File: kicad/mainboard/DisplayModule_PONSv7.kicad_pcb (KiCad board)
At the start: 4 copper layers, 55.4 x 77.6 mm, 135 parts, among them J1 Ext. Speaker, J2 54132-4062, J3 2005280040, J4 Micro_SD_Card_Det2, J5 Conn_01x03_Shielded, J6 USB_B_Micro, Q1 AO3401A, SW1 PTS645VK392LFS, SW2 SW_TS-1088, SW3 SW_TS-1088, U1 PAM8302AADCR, U10 BNO085, U12 E220-900T22S(JP), U2 W25Q128JVS, U3 RP2350_80QFN, U4 MCP73831-2-OT, U5 TPS63031DSK, U6 MAINSW_CUS-12TB, U7 TFTSW_CUS-12TB, U8 MS5611-01BA, Y1 X322512MSB4SI, Y2 32.768k

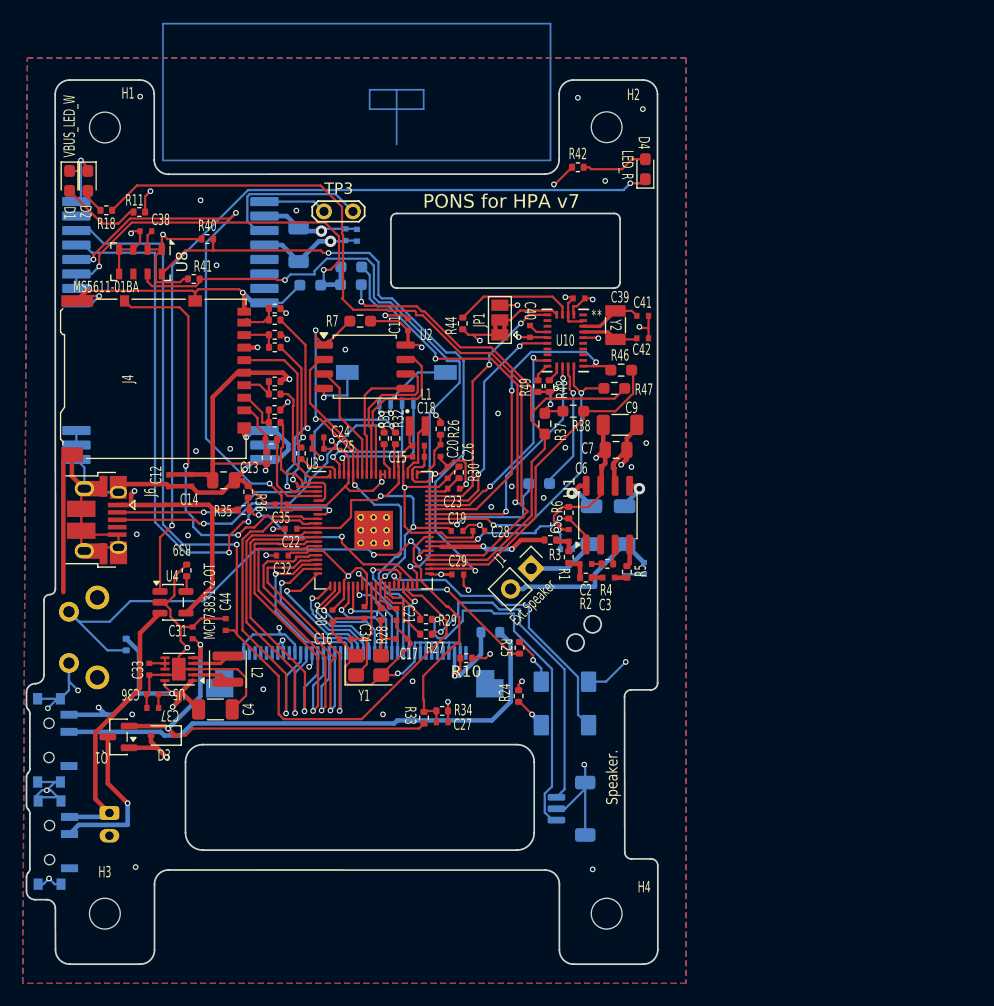
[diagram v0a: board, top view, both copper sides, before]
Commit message: 0.962 KiCad 更新、production を git 管理から外す
fabrication-toolkit が生成する production/ は発注のたびに作り直せるうえ、
基板を直すたびに巨大な差分になるので .gitignore に追加した。

Co-Authored-By: Claude Opus 5 <noreply@anthropic.com>
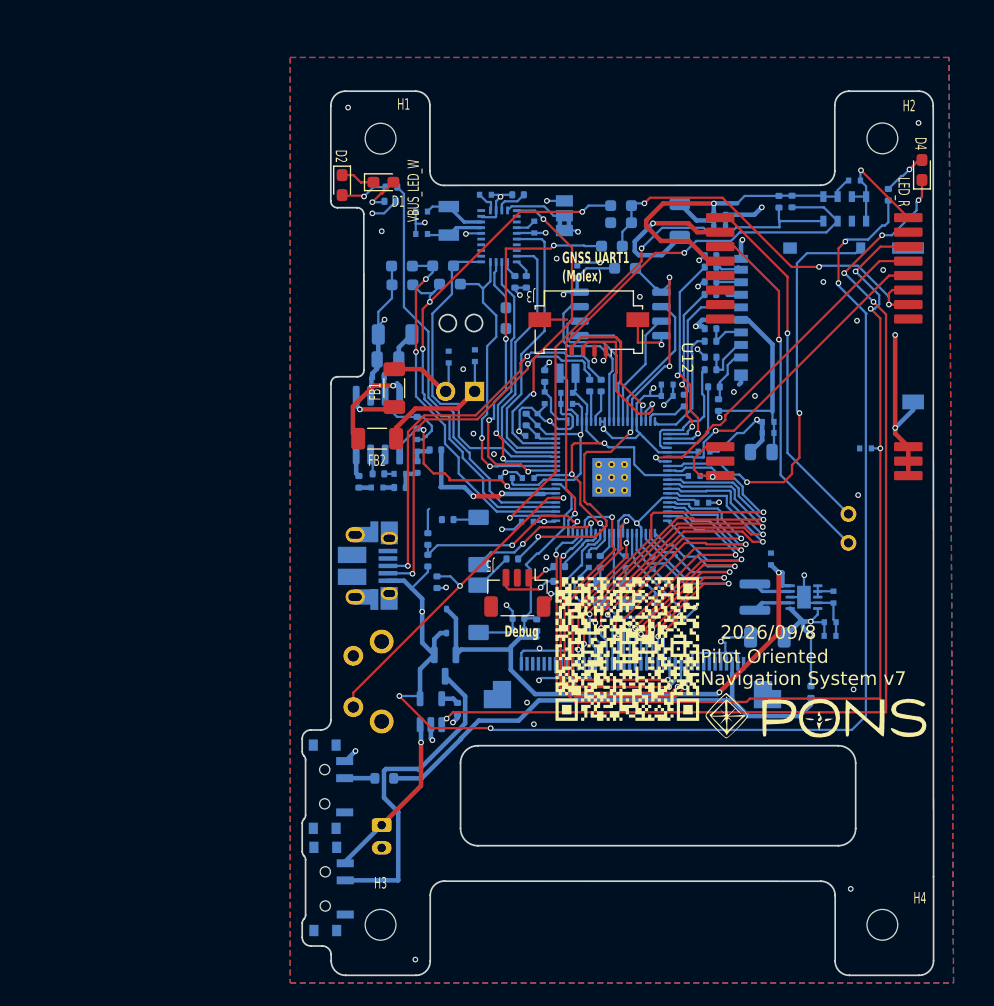
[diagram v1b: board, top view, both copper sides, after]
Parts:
- C11, C12, C13, C14, C15, C16, C17, C18, C19, C2, C20, C21, C22, C23, C24, C25, C26, C27, C28, C29, C3, C30, C31, C32, C33, C34, C35, C36, C37, C38, C39, C4, C40, C41, C42, C44, C5, C6, C7, C9, D3, J1, J4, J6, JP1, L1, L2, Q1, R1, R10, R11, R12, R13, R14, R15, R16, R17, R18, R19, R2, R20, R21, R22, R23, R24, R25, R26, R27, R28, R29, R3, R30, R31, R32, R33, R34, R35, R36, R37, R38, R39, R4, R40, R41, R42, R44, R46, R47, R48, R49, R5, R6, R7, TP3, U1, U10, U2, U3, U4, U5, U8, Y1, Y2: moved to B.Cu
- FB1, FB2, G*** (x2), J3, J5, U12: moved to F.Cu
- moved C38 62.3 mm to (143.6, 62.6), turned to 0 degrees
- moved U8 62.0 mm to (142.7, 65.0)
- moved C33 60.4 mm to (141.7, 99.1)
- moved C36 59.8 mm to (141.4, 101.3), turned to 0 degrees
- moved C37 59.8 mm to (141.4, 102.5), turned to 0 degrees
- moved J4 59.2 mm to (141.3, 75.3)
- moved C44 58.2 mm to (144.5, 86.1), turned to 180 degrees
- moved U12 56.5 mm to (140.0, 88.5), turned to 0 degrees
- moved U5 55.2 mm to (139.1, 99.1), turned to 0 degrees
- moved TP3 53.1 mm to (143.0, 91.8), turned to -90 degrees
- moved R41 52.9 mm to (138.1, 64.4), turned to -90 degrees
- moved C12 52.7 mm to (136.0, 84.7), turned to 180 degrees
- moved C31 51.2 mm to (136.2, 95.8)
- moved C14 50.9 mm to (136.0, 83.7), turned to 180 degrees
- moved R40 50.3 mm to (136.9, 64.4), turned to -90 degrees
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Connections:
- SW1 pad 1: SW_TOGGLE -> GND
- SW1 pad 2: GND -> SW_TOGGLE
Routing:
- net GND: track 293.0 -> 199.7 mm, vias 61 -> 49
- net PWR_TFT: track 46.9 -> 2.66 mm
- net Net-(J2-Pad3): track 8.80 -> 44.3 mm, vias 1 -> 0
- net USR_LED: track 70.6 -> 36.8 mm
- net Net-(J5-Pin_1): track 31.1 -> 2.57 mm
- net Net-(U12-SWDIO): track 5.58 -> 31.1 mm, vias 0 -> 1
- net Net-(J5-Pin_3): track 28.1 -> 5.34 mm
- net UART1_TX: track 50.0 -> 28.6 mm, vias 3 -> 1
- net TFT_RESET: track 6.64 -> 27.9 mm, vias 1 -> 2
- net UART1_RX: track 51.3 -> 30.8 mm, vias 3 -> 1
- net DB15: track 12.6 -> 32.7 mm, vias 1 -> 2
- net DB14: track 9.56 -> 28.6 mm, vias 1 -> 2
- net Net-(D4-K): track 73.7 -> 91.1 mm, vias 2 -> 5
- net Net-(U12-SWCLK): track 14.0 -> 31.4 mm, vias 0 -> 1
- net VBUS: track 142.4 -> 159.6 mm, vias 4 -> 6
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- added copper zone on In1.Cu, net +3V3
- added copper zone on In2.Cu, net GND
- removed copper zone on In2.Cu, net +3V3
- removed copper zone on In1.Cu, net GND
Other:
- outline, holes or cut-outs redrawn
- board text added: "2026/09/8"
- board text added: "[Memo JLCPCB BOM Exemption] J1 Speaker socket (No parts required) J5 Debug SH 3p(No use. Debug purpose) U12 E220 LoRa (Due to 技適, 手実装) U6,U7 CUS-12TB Switch (JLCPCBにないパーツのため手実装） H1,H2,H3,H4 Hole TP3 LoRa JP SW1 (JLCにないパーツのため） PWR1（コスト） Not an assemble parts JP1 I2C-SPI jumper BNO085 R47,R7,R46,R38,R37,R50,R51 DNF"
- board text removed: "2026/09/5"
- board text removed: "Ext.Speaker"
- board text removed: "[Memo JLCPCB BOM Exemption] J1 Speaker socket (No parts required) J5 Debug SH 3p(No use. Debug purpose) U12 E220 LoRa (Due to 技適) U6,U7 CUS-12TB Switch H1,H2,H3,H4 Hole TP3 LoRa JP"
